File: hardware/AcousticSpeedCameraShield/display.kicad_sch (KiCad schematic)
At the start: 8 parts

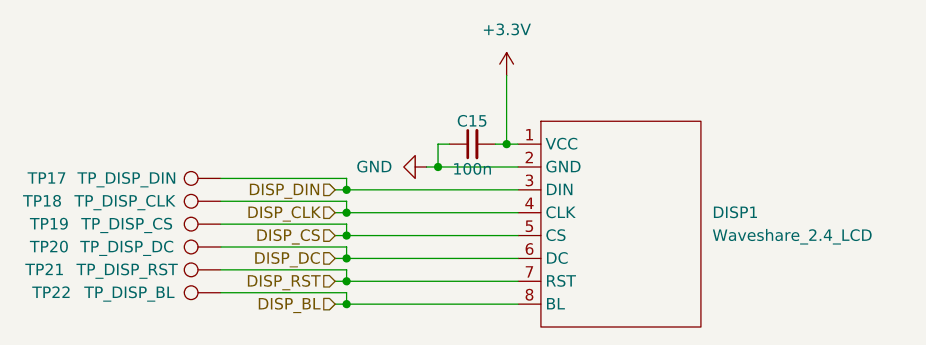
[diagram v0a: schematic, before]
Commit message: update MCU pin assignments
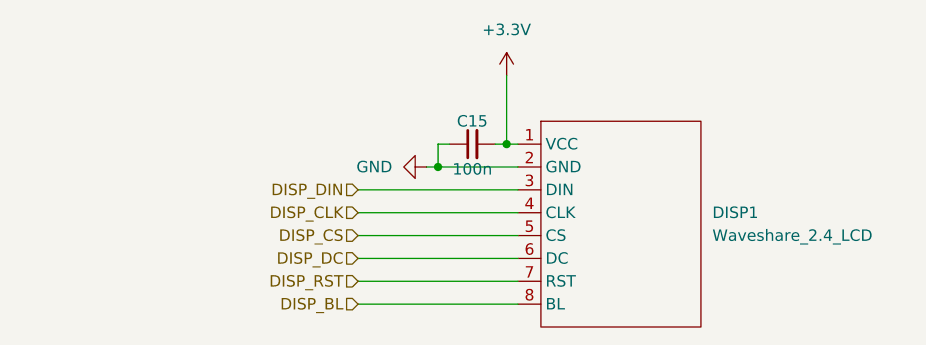
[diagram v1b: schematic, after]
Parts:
- removed TP17: TP_DISP_DIN, symbol Connector:TestPoint
- removed TP18: TP_DISP_CLK, symbol Connector:TestPoint
- removed TP19: TP_DISP_CS, symbol Connector:TestPoint
- removed TP20: TP_DISP_DC, symbol Connector:TestPoint
- removed TP21: TP_DISP_RST, symbol Connector:TestPoint
- removed TP22: TP_DISP_BL, symbol Connector:TestPoint
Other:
- title: (none) -> Interfejs Wyświetlacza
